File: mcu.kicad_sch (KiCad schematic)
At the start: 36 parts, among them J1 USB_B_Micro, J6 SM03B-SRSS-TB, SW10 SW_Push, SW9 SW_Push, U2 NCP1117-3.3_SOT223, U3 W25Q128JVS, U4 RP2350_60QFN, Y1 ABM8-272-T3

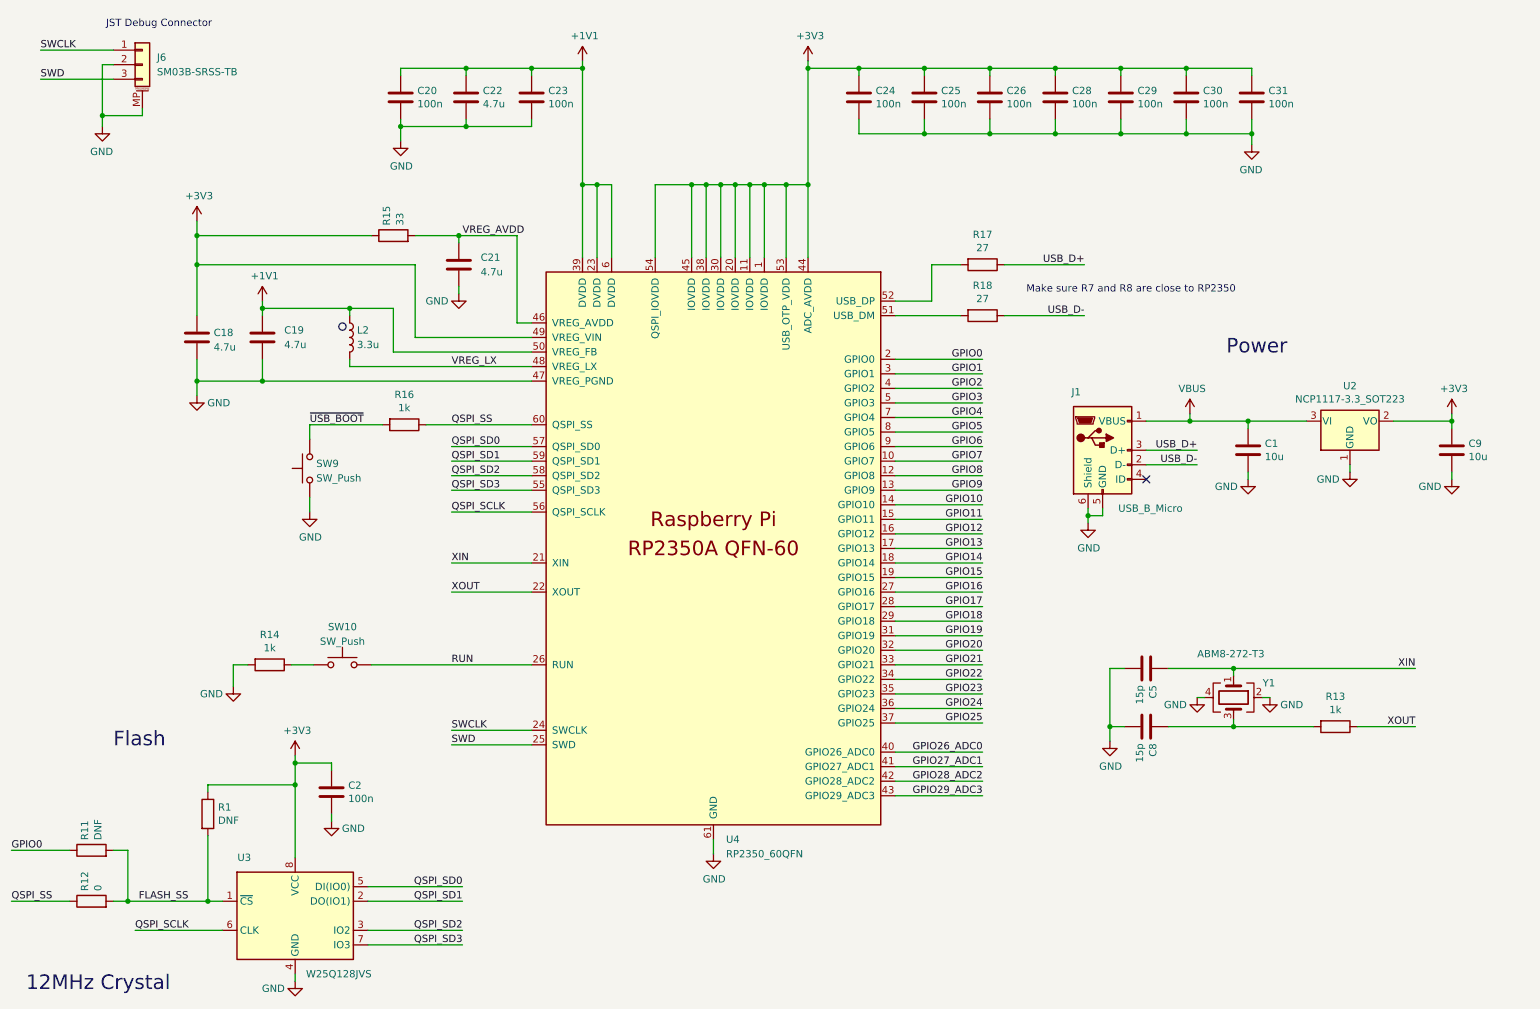
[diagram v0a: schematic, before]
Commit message: add usb c connector
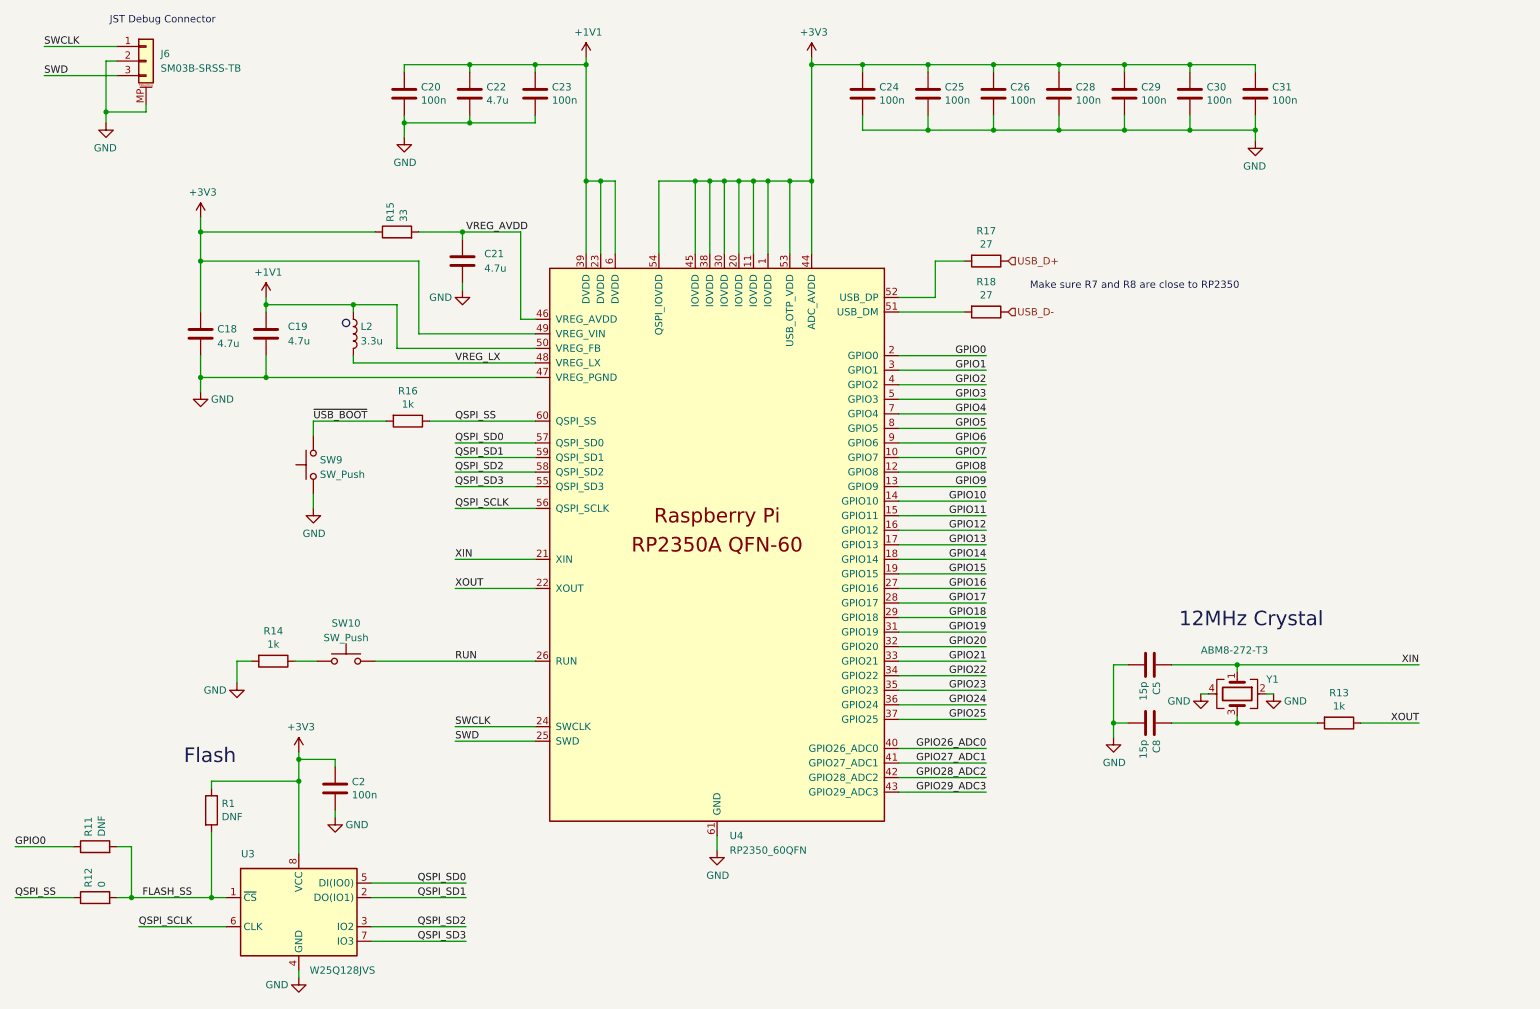
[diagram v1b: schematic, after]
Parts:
- removed C1, C9: 10u, Capacitor_SMD:C_0805_2012Metric, symbol Device:C
- removed J1: USB_B_Micro, Connector_USB:USB_Micro-B_Amphenol_10103594-0001LF_Horizontal, symbol Connector:USB_B_Micro
- removed U2: NCP1117-3.3_SOT223, Package_TO_SOT_SMD:SOT-223-3_TabPin2, symbol Regulator_Linear:NCP1117-3.3_SOT223
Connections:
- no-connect marks 1 -> 0
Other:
- note removed: "Power"
- moved on the sheet: C18, C19, C2, C20, C21, C22, C23, C24, C25, C26, C28, C29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

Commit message: schematic functional and includes current test setup
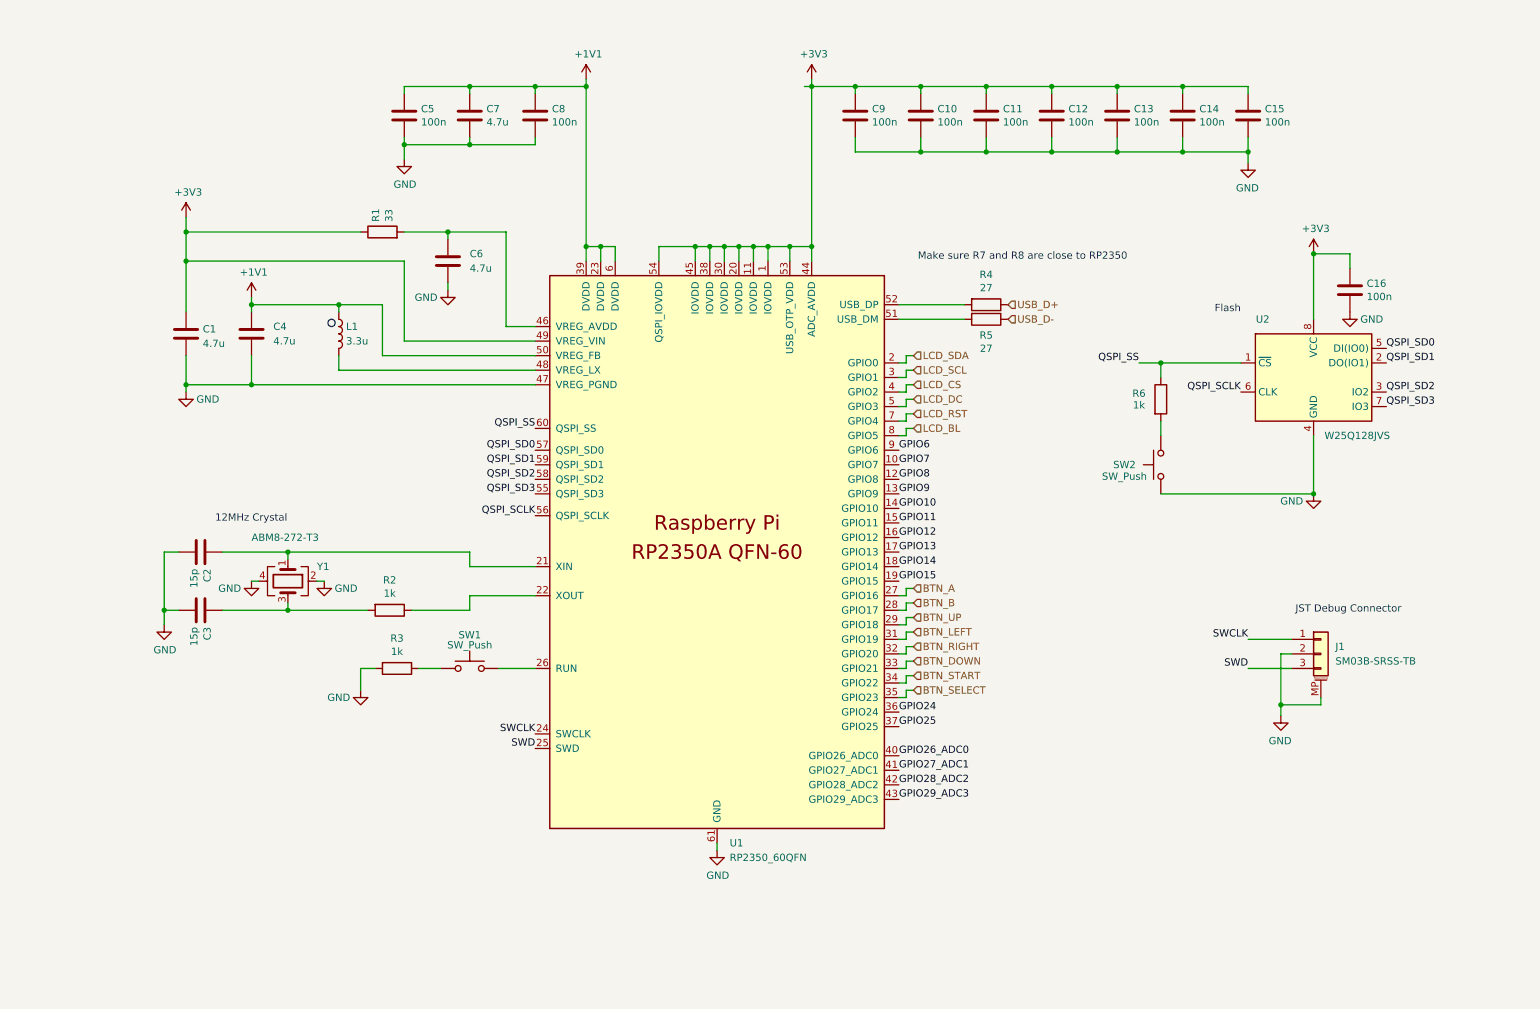
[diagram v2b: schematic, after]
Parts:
- removed R1, R11: DNF, Resistor_SMD:R_0402_1005Metric, symbol Device:R
- removed R12: 0, Resistor_SMD:R_0402_1005Metric, symbol Device:R
- removed R16: 1k, Resistor_SMD:R_0402_1005Metric, symbol Device:R
- removed SW9: SW_Push, Button_Switch_SMD:SW_Push_1P1T_NO_Vertical_Wuerth_434133025816, symbol Switch:SW_Push
- added R6: 1k, Resistor_SMD:R_0402_1005Metric, symbol Device:R
- added SW2: SW_Push, Button_Switch_SMD:SW_Push_1P1T_NO_Vertical_Wuerth_434133025816, symbol Switch:SW_Push
- renumbered C18 to C1, C25 to C10, C26 to C11, C28 to C12, C29 to C13, C30 to C14, C31 to C15, C2 to C16, C5 to C2, C8 to C3, C19 to C4, C20 to C5, C21 to C6, C22 to C7, C23 to C8, C24 to C9, J6 to J1, L2 to L1, R15 to R1, R13 to R2, R14 to R3, R17 to R4, R18 to R5, SW10 to SW1, U4 to U1, U3 to U2
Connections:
- net FLASH_SS is gone; now on net QSPI_SS: U2.1 (~{CS})
- net GND: now also SW2.1
- net QSPI_SS: now also R6.1
- net GPIO0 renamed LCD_SDA
- net GPIO1 renamed LCD_SCL
- net GPIO16 renamed BTN_A
- net GPIO17 renamed BTN_B
- net GPIO18 renamed BTN_UP
- net GPIO19 renamed BTN_LEFT
- net GPIO2 renamed LCD_CS
- net GPIO20 renamed BTN_RIGHT
- net GPIO21 renamed BTN_DOWN
- net GPIO22 renamed BTN_START
- net GPIO23 renamed BTN_SELECT
- net GPIO3 renamed LCD_DC
- net GPIO4 renamed LCD_RST
- net GPIO5 renamed LCD_BL
- net RUN: no longer names the net of SW1.2, U1.26 (RUN)
- net VREG_AVDD: no longer names the net of C6.1, R1.2, U1.46 (VREG_AVDD)
- net VREG_LX: no longer names the net of L1.2, U1.48 (VREG_LX)
- net XIN: no longer names the net of C2.1, U1.21 (XIN), Y1.1
- net XOUT: no longer names the net of R2.1, U1.22 (XOUT)
- new net: R6.2, SW2.2
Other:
- moved on the sheet: C1, C10, C11, C12, C13, C14, C15, C16, C2, C3, C4, C5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

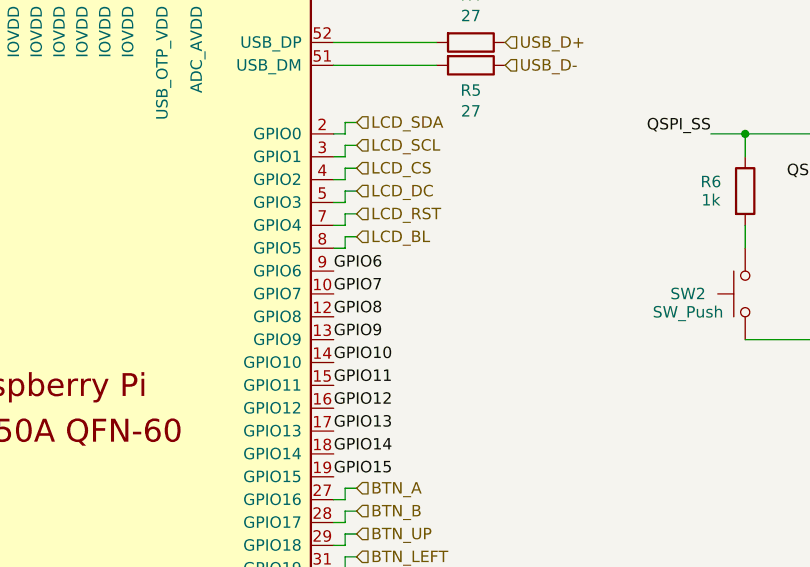
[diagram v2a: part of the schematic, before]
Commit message: add audio amp
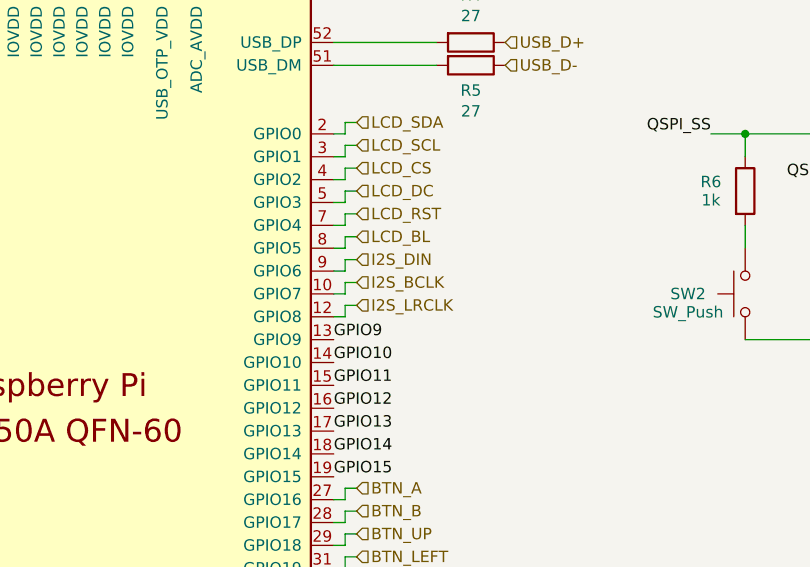
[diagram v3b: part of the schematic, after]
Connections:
- net GPIO6 renamed I2S_DIN
- net GPIO7 renamed I2S_BCLK
- net GPIO8 renamed I2S_LRCLK
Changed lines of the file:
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@@
+	(wire
+		(pts
+			(xy 176.53 99.06) (xy 175.26 99.06)
+		)
+		(stroke
+			(width 0)
+			(type default)
+		)
+	)
 	(wire
 		(pts
@@
 	(wire
 		(pts
+			(xy 176.53 95.25) (xy 177.8 95.25)
+		)
+		(stroke
+			(width 0)
+			(type default)
+		)
+	)
+	(wire
+		(pts
 			(xy 176.53 77.47) (xy 177.8 77.47)
 		)
@@
 	(wire
 		(pts
+			(xy 176.53 95.25) (xy 176.53 96.52)
+		)
+		(stroke
+			(width 0)
+			(type default)
+		)
+	)
+	(wire
+		(pts
 			(xy 133.35 60.96) (xy 133.35 58.42)
 		)
@@
 	(wire
 		(pts
+			(xy 176.53 97.79) (xy 176.53 99.06)
+		)
+		(stroke
+			(width 0)
+			(type default)
+		)
+	)
+	(wire
+		(pts
 			(xy 111.76 40.64) (xy 111.76 39.37)
 		)
@@
 	(wire
 		(pts
+			(xy 176.53 97.79) (xy 177.8 97.79)
+		)
+		(stroke
+			(width 0)
+			(type default)
+		)
+	)
+	(wire
+		(pts
 			(xy 176.53 120.65) (xy 176.53 121.92)
 		)
@@
 	(wire
 		(pts
+			(xy 176.53 96.52) (xy 175.26 96.52)
+		)
+		(stroke
+			(width 0)
+			(type default)
+		)
+	)
+	(wire
+		(pts
 			(xy 224.79 31.75) (xy 224.79 30.48)
 		)
@@
 	(wire
 		(pts
+			(xy 176.53 92.71) (xy 177.8 92.71)
+		)
+		(stroke
+			(width 0)
+			(type default)
+		)
+	)
+	(wire
+		(pts
 			(xy 179.07 31.75) (xy 179.07 30.48)
 		)
@@
 	(wire
 		(pts
+			(xy 176.53 93.98) (xy 175.26 93.98)
+		)
+		(stroke
+			(width 0)
+			(type default)
+		)
+	)
+	(wire
+		(pts
 			(xy 176.53 87.63) (xy 176.53 88.9)
 		)
@@
 		(pts
 			(xy 62.23 69.85) (xy 62.23 68.58)
+		)
+		(stroke
+			(width 0)
+			(type default)
+		)
+	)
+	(wire
+		(pts
+			(xy 176.53 92.71) (xy 176.53 93.98)
 		)
 		(stroke
@@
 		)
 	)
-	(label "GPIO6"
-		(at 175.26 93.98 0)
-		(effects
-			(font
-				(size 1.27 1.27)
-			)
-			(justify left bottom)
-		)
-	)
 	(label "QSPI_SD2"
 		(at 111.76 99.06 180)
@@
 		)
 	)
-	(label "GPIO7"
-		(at 175.26 96.52 0)
-		(effects
-			(font
-				(size 1.27 1.27)
-			)
-			(justify left bottom)
-		)
-	)
 	(label "GPIO12"
 		(at 175.26 109.22 0)
@@
 			)
 			(justify right bottom)
-		)
-	)
-	(label "GPIO8"
-		(at 175.26 99.06 0)
-		(effects
-			(font
-				(size 1.27 1.27)
-			)
-			(justify left bottom)
 		)
 	)
@@
 		)
 	)
+	(hierarchical_label "I2S_DIN"
+		(shape input)
+		(at 177.8 92.71 0)
+		(effects
+			(font
+				(size 1.27 1.27)
+			)
+			(justify left)
+		)
+	)
 	(hierarchical_label "LCD_BL"
 		(shape input)
@@
 		)
 	)
+	(hierarchical_label "I2S_LRCLK"
+		(shape input)
+		(at 177.8 97.79 0)
+		(effects
+			(font
+				(size 1.27 1.27)
+			)
+			(justify left)
+		)
+	)
 	(hierarchical_label "USB_D+"
 		(shape input)
@@
 		(effects
 			(font
+				(size 1.27 1.27)
+			)
+			(justify left)
+		)
+	)
+	(hierarchical_label "I2S_BCLK"
+		(shape input)
+		(at 177.8 95.25 0)
+		(effects
+			(font
